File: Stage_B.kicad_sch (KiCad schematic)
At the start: 0 parts

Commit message: skdja7rkweg
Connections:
- no-connect marks 0 -> 3
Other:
- sheet POWER AMP1 ports: added VCC, power detect; removed none
- sheet POWER AMP2 ports: added VCC; removed none
- sheet POWER AMP3 ports: added VCC, power detect; removed none
- sheet POWER AMP4 ports: added VCC; removed none
- sheet POWER AMP5 ports: added VCC, power detect; removed none
- sheet POWER AMP6 ports: added VCC; removed none

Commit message: moving along
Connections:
- no-connect marks 3 -> 2
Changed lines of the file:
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@@
-	)
-	(no_connect
-		(at 208.28 93.98)
 	)
 	(no_connect
@@
 		)
 	)
+	(global_label "Stage_2_power"
+		(shape input)
+		(at 208.28 93.98 0)
+		(fields_autoplaced yes)
+		(effects
+			(font
+				(size 1.27 1.27)
+			)
+			(justify left)
+		)
+		(property "Intersheetrefs" "${INTERSHEET_REFS}"
+			(at 225.235 93.98 0)
+			(hide yes)
+			(show_name no)
+			(do_not_autoplace no)
+			(effects
+				(font
+					(size 1.27 1.27)
+				)
+				(justify left)
+			)
+		)
+	)
+	(global_label "Stage_2_power"
+		(shape input)
+		(at 350.52 148.59 0)
+		(fields_autoplaced yes)
+		(effects
+			(font
+				(size 1.27 1.27)
+			)
+			(justify left)
+		)
+		(property "Intersheetrefs" "${INTERSHEET_REFS}"
+			(at 367.475 148.59 0)
+			(hide yes)
+			(show_name no)
+			(do_not_autoplace no)
+			(effects
+				(font
+					(size 1.27 1.27)
+				)
+				(justify left)
+			)
+		)
+	)

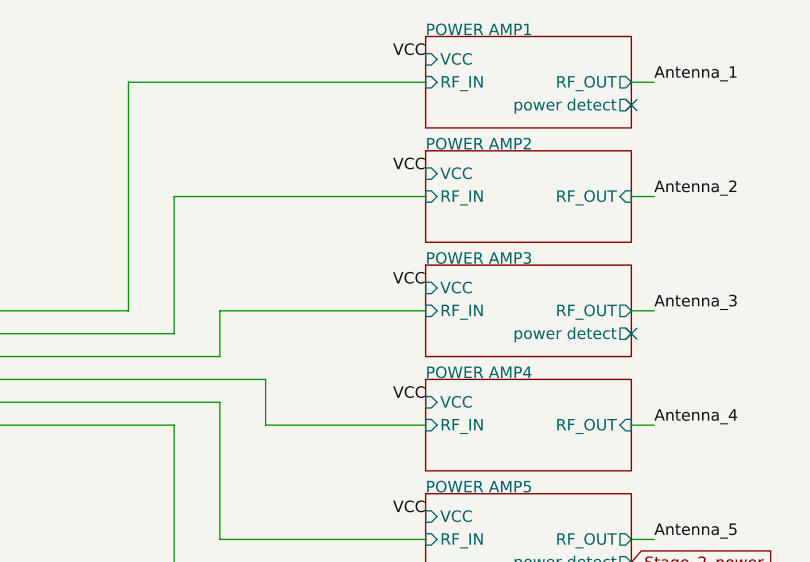
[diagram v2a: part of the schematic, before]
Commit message: 6 layers now
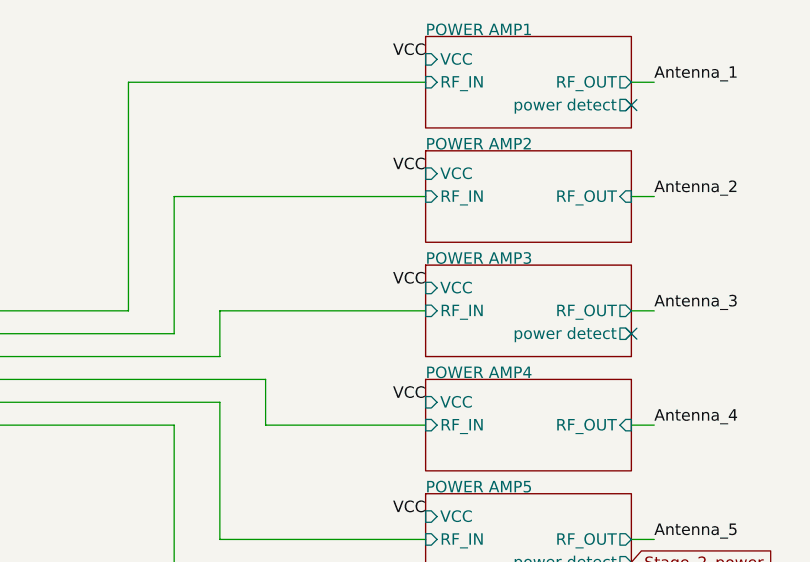
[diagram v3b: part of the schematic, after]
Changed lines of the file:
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@@
 	)
 	(label "VCC"
-		(at 185.4066 63.5 180)
+		(at 185.42 63.5 180)
 		(effects
 			(font

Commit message: june_26
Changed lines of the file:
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@@
+	(wire
+		(pts
+			(xy 208.28 93.98) (xy 218.44 93.98)
+		)
+		(stroke
+			(width 0)
+			(type default)
+		)
+	)
 	(wire
 		(pts
@@
 			)
 			(justify right bottom)
-		)
-	)
-	(global_label "Stage_2_power"
-		(shape input)
-		(at 208.28 93.98 0)
-		(fields_autoplaced yes)
-		(effects
-			(font
-				(size 1.27 1.27)
-			)
-			(justify left)
-		)
-		(property "Intersheetrefs" "${INTERSHEET_REFS}"
-			(at 225.235 93.98 0)
-			(hide yes)
-			(show_name no)
-			(do_not_autoplace no)
-			(effects
-				(font
-					(size 1.27 1.27)
-				)
-				(justify left)
-			)
-		)
-	)
-	(global_label "Stage_2_power"
-		(shape input)
-		(at 350.52 148.59 0)
-		(fields_autoplaced yes)
-		(effects
-			(font
-				(size 1.27 1.27)
-			)
-			(justify left)
-		)
-		(property "Intersheetrefs" "${INTERSHEET_REFS}"
-			(at 367.475 148.59 0)
-			(hide yes)
-			(show_name no)
-			(do_not_autoplace no)
-			(effects
-				(font
-					(size 1.27 1.27)
-				)
-				(justify left)
-			)
 		)
 	)
@@
 		)
 	)
+	(hierarchical_label "power_det"
+		(shape output)
+		(at 218.44 93.98 0)
+		(effects
+			(font
+				(size 1.27 1.27)
+			)
+			(justify left)
+		)
+	)
